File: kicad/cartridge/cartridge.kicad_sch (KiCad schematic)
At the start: 11 parts, among them J1 Card edge (87715-9106 mate), U1 ATF22V10C-10PU, U2 AT28C256-15PU, U3 AT28C256-15PU, U4 AS7C256C-15PCN, U5 AS7C256C-15PCN

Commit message: KiCad schematic: wire each sheet's nets, one routed bus per bus, PLD names
A net with two or more pins on a sheet is now wired pin to pin by a small
grid router (src/scripts/kicad_route.py) instead of a label per pin.
Numbered groups (D, A, SRC, PC, ...) are drawn as one bus per sheet with
bus entries, routed between the chips and named by one bus label.  Each
PLD shows its job under its part number.  Netlist check: 0 problems.

Co-Authored-By: Claude Opus 5.5 (1M context) <noreply@anthropic.com>
Claude-Session: https://claude.ai/code/session_01L9AkLuEg13EebxDmgXsaEp
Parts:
- U1: Function (none) -> Loader PLD
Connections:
- net HOLD: no longer names the net of J1.B18 (HOLD), U1.23 (/RELEASE)
- net OSC: no longer names the net of J1.A20 (OSC), U1.1 (OSC)
- net PIXEL_ENABLE: no longer names the net of J1.A18 (PIXEL_ENABLE), U1.3 (PIXEL_ENABLE)
- net RUN: no longer names the net of J1.A19 (RUN), U1.22 (RUN)
- net ~{CE_HI}: no longer names the net of J1.B16 (/CE_HI), U3.20 (~{CS}), U5.20 (/CE)
- net ~{CE_LO}: no longer names the net of J1.A16 (/CE_LO), U1.2 (A15), U2.20 (~{CS}), U4.20 (/CE)
- net ~{EE_OE}: no longer names the net of U1.20 (/EE_OE), U2.22 (~{OE}), U3.22 (~{OE})
- net ~{ROM_OE}: no longer names the net of J1.A17 (/ROM_OE), U4.22 (/OE), U5.22 (/OE)
- net ~{SRC_EN}: no longer names the net of J1.B17 (/SRC_EN), U1.4 (/SRC_EN)
- net ~{SR_WE}: no longer names the net of U1.19 (/SR_WE), U4.27 (/WE), U5.27 (/WE)

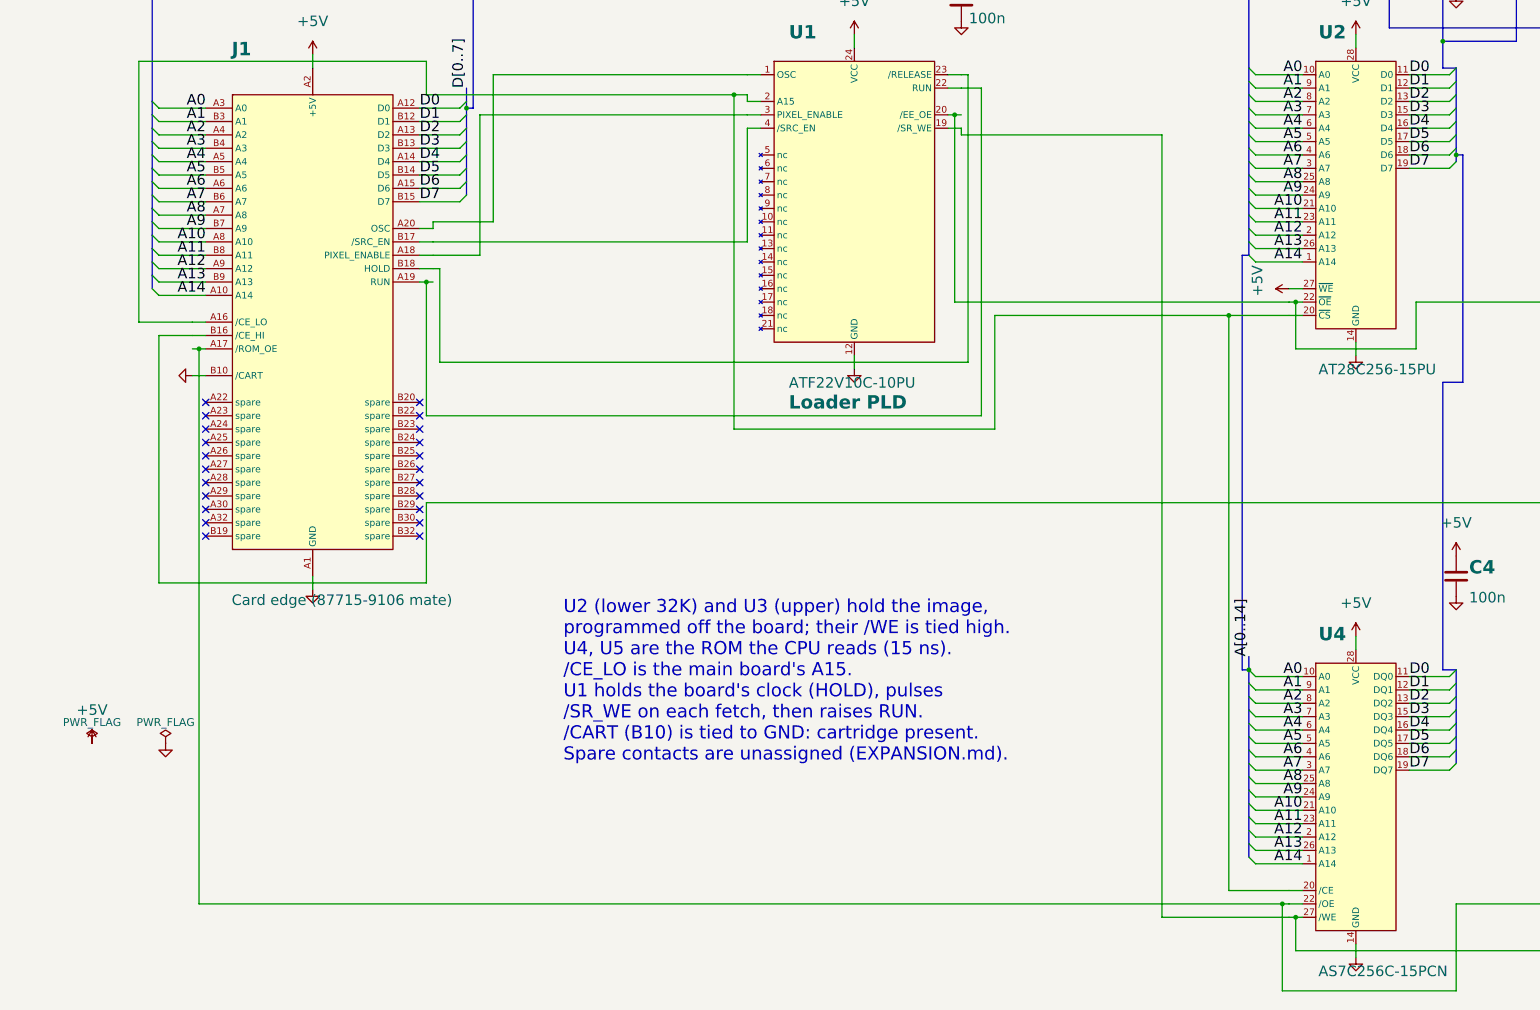
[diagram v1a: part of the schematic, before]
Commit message: Revert the opcode XOR: plain encoding, the cartridge 74AC541 is back
Justin found the inverted opcode bytes too confusing, and a pulled-low
bus is not practical, so this undoes 63a428c:
- opcode bytes are the plain fields again (nop = 02h); the cartridge's
  74AC541 drives 02h while it loads (6 chips, about 33 ms)
- State and Branch PLD revision 15, ALU revision 07 and cartridge PLD
  revision 03 have the same logic as 13, 13, 05 and 01
- read bus pull-ups 10k again; bring-up colour pull-downs 1k
- cartridge schematic gets U6 (74AC541), data bus SIP 10k
- program hex, menu ROM and bring-up ROM reassembled

Kept from 63a428c: RUN starts high in basys_top, the bring-up ROM's
explicit jump to frame_loop, and test_io's con_gets ROM map.

Co-Authored-By: Claude Opus 5.5 (1M context) <noreply@anthropic.com>
Claude-Session: https://claude.ai/code/session_01PNJoPfzmo1tu8EorCrua96
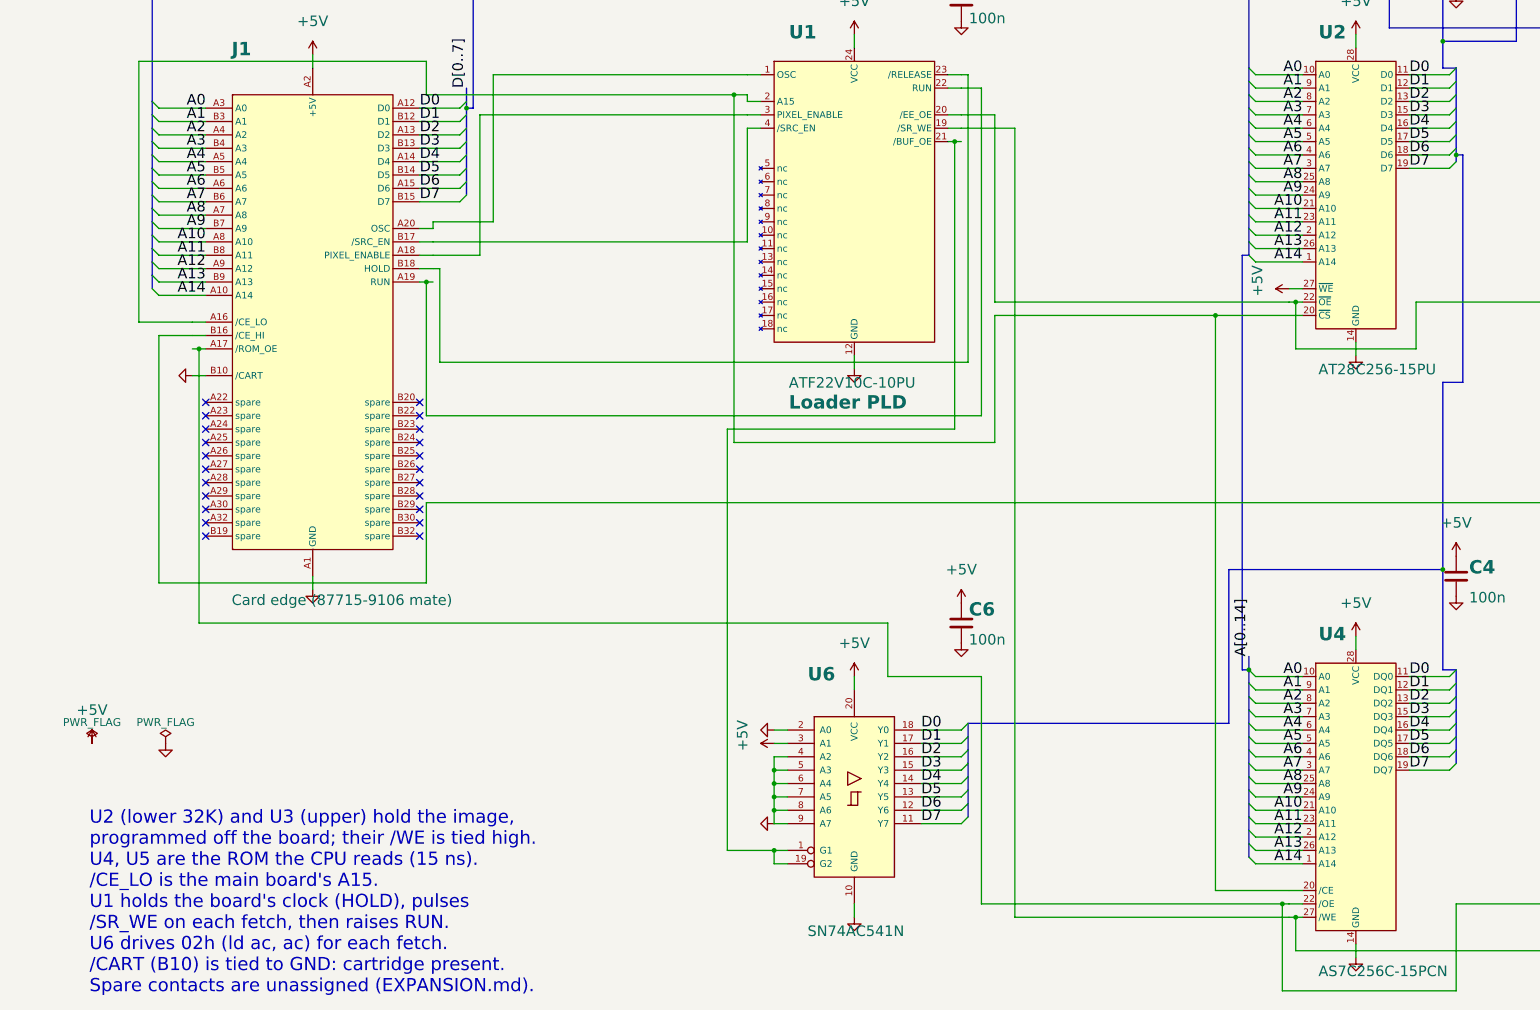
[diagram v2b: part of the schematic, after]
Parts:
- added C6: 100n, Capacitor_THT:C_Disc_D5.0mm_W2.5mm_P5.00mm, symbol Device:C
- added U6: SN74AC541N, Package_DIP:DIP-20_W7.62mm, symbol 74xx:74LS541
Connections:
- net +5V: now also C6.1, U6.20 (VCC), U6.3 (A1)
- net D0: now also U6.18 (Y0)
- net D1: now also U6.17 (Y1)
- net D2: now also U6.16 (Y2)
- net D3: now also U6.15 (Y3)
- net D4: now also U6.14 (Y4)
- net D5: now also U6.13 (Y5)
- net D6: now also U6.12 (Y6)
- net D7: now also U6.11 (Y7)
- net GND: now also C6.2, U6.10 (GND), U6.2 (A0), U6.4 (A2), U6.5 (A3), U6.6 (A4), U6.7 (A5), U6.8 (A6), U6.9 (A7)
- net at U1.21 (/BUF_OE): now also U6.1 (G1), U6.19 (G2)
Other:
- note added: "U6 drives 02h (ld ac, ac) for each fetch."

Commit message: Cartridge loader everywhere: FPGA cartridge model, random RAM, nop at x0000
- src/hdl/cartridge.vhd: the ROM cartridge (loader PLD, EEPROMs from
  rom.mem, SRAM written by /SR_WE); basys_top uses it for RUN, STALL_OUT
  and the ROM data, and the IR PLD replaces the instruction F377
- main RAM and cartridge SRAM start random (gen_random_ram.tcl writes
  ram.mem and cart_ram.mem); build, fast and create_project scripts
  updated, new .vhd files are added to an existing project
- rom_boot and the bring-up ROM keep a nop at x0000 for the hand-off;
  menu and bring-up images rebuilt
- schematic: IR PLD as U17, no 74AC32, STALL_IN/STALL_OUT/PC_ENABLE on
  the cartridge connector, cartridge without the 541; PDFs regenerated
- docs: ROM, CHIPS, BRINGUP, EXPANSION, timing, PLD usage, kitting,
  schematic plan, block diagram
- src/sim/tb_top_load.vhd: whole FPGA model from power-up through the
  load and boot

Co-Authored-By: Claude Opus 5.5 (1M context) <noreply@anthropic.com>
Claude-Session: https://claude.ai/code/session_01PNJoPfzmo1tu8EorCrua96
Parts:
- removed C6: 100n, Capacitor_THT:C_Disc_D5.0mm_W2.5mm_P5.00mm, symbol Device:C
- removed U6: SN74AC541N, Package_DIP:DIP-20_W7.62mm, symbol 74xx:74LS541
- U1: value ATF22V10C-10PU -> ATF22V10C-7PX
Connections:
- net at J1.B17 (STALL_IN): now also U1.5 (STALL_IN); no longer U1.4 (/SRC_EN)
- net at J1.B19 (PC_ENABLE): now also U1.4 (PC_ENABLE)
- no-connect marks 22 -> 21
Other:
- note added: "(STALL_OUT), pulses /SR_WE, lets the CPU"
- note added: "U1 stalls the CPU at each PC address"
- note added: "step, and raises RUN when the PC wraps."
- note removed: "/SR_WE on each fetch, then raises RUN."
- note removed: "U1 holds the board's clock (HOLD), pulses"
- note removed: "U6 drives 02h (ld ac, ac) for each fetch."

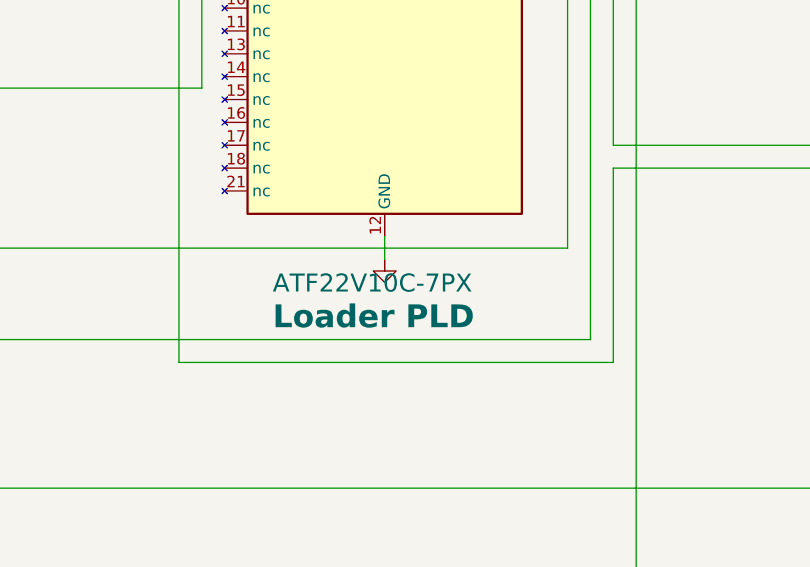
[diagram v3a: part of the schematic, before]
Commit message: Branch, audio slot and cartridge PLDs to ATF22V10C-10PU
The IR PLD's 5.5 ns clock to output gave the IR-started paths 5 ns, so
the Branch PLD (+4.7 branch decision, +2.2 STALL through the cartridge)
and the audio slot PLD (+5.2 /AC_SEL) fit the -10 grade; the cartridge
loader goes with them (tb_cart_load passes with every PLD at -10).

Co-Authored-By: Claude Opus 5.5 (1M context) <noreply@anthropic.com>
Claude-Session: https://claude.ai/code/session_01PNJoPfzmo1tu8EorCrua96
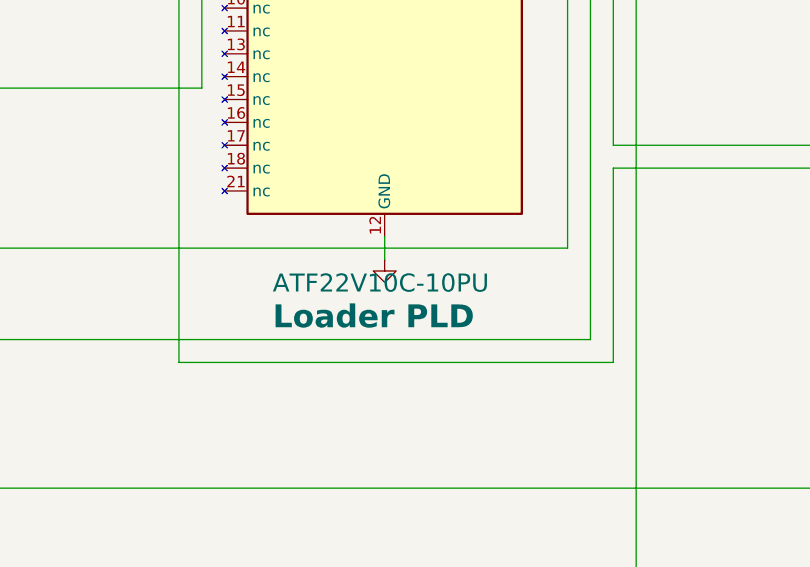
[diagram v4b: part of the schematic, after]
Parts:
- U1: value ATF22V10C-7PX -> ATF22V10C-10PU
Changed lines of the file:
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@@
   (wire (pts (xy 175.26 125.73) (xy 175.26 128.27)) (stroke (width 0) (type default)))
   (symbol (lib_id "power:GND") (at 175.26 128.27 0) (unit 1) (in_bom yes) (on_board yes) (dnp no) (property "Reference" "#PWR0105" (at 175.26 128.27 0) (effects (font (size 1.27 1.27)) hide)) (property "Value" "GND" (at 175.26 134.62 0) (effects (font (size 2 2)) hide)) (property "Footprint" "" (at 175.26 128.27 0) (effects (font (size 1.27 1.27)) hide)) (property "Datasheet" "" (at 175.26 128.27 0) (effects (font (size 1.27 1.27)) hide)) (pin "1") (instances (project "cartridge" (path "/58e6aaf0-b096-58ec-a49b-041f90960c95" (reference "#PWR0105") (unit 1)))))
-  (symbol (lib_id "placard:ATF22V10C_CART") (at 175.26 95.25 0) (unit 1) (in_bom yes) (on_board yes) (dnp no) (property "Reference" "U1" (at 162.814 63.27 0) (effects (font (size 2.54 2.54) bold) (justify left bottom))) (property "Value" "ATF22V10C-7PX" (at 162.814 129.73 0) (effects (font (size 2 2)) (justify left top))) (property "Function" "Loader PLD" (at 162.814 133.13 0) (effects (font (size 2.54 2.54) bold) (justify left top))) (property "Footprint" "Package_DIP:DIP-24_W7.62mm" (at 175.26 95.25 0) (effects (font (size 1.27 1.27)) hide)) (property "Datasheet" "https://ww1.microchip.com/downloads/en/DeviceDoc/doc0735.pdf" (at 175.26 95.25 0) (effects (font (size 1.27 1.27)) hide)) (property "PLD" "ATF22V10_CART.pld" (at 175.26 95.25 0) (effects (font (size 1.27 1.27)) hide)) (pin "1") (pin "2") (pin "3") (pin "4") (pin "5") (pin "6") (pin "7") (pin "8") (pin "9") (pin "10") (pin "11") (pin "13") (pin "14") (pin "15") (pin "16") (pin "17") (pin "18") (pin "21") (pin "22") (pin "20") (pin "19") (pin "23") (pin "24") (pin "12") (instances (project "cartridge" (path "/58e6aaf0-b096-58ec-a49b-041f90960c95" (reference "U1") (unit 1)))))
+  (symbol (lib_id "placard:ATF22V10C_CART") (at 175.26 95.25 0) (unit 1) (in_bom yes) (on_board yes) (dnp no) (property "Reference" "U1" (at 162.814 63.27 0) (effects (font (size 2.54 2.54) bold) (justify left bottom))) (property "Value" "ATF22V10C-10PU" (at 162.814 129.73 0) (effects (font (size 2 2)) (justify left top))) (property "Function" "Loader PLD" (at 162.814 133.13 0) (effects (font (size 2.54 2.54) bold) (justify left top))) (property "Footprint" "Package_DIP:DIP-24_W7.62mm" (at 175.26 95.25 0) (effects (font (size 1.27 1.27)) hide)) (property "Datasheet" "https://ww1.microchip.com/downloads/en/DeviceDoc/doc0735.pdf" (at 175.26 95.25 0) (effects (font (size 1.27 1.27)) hide)) (property "PLD" "ATF22V10_CART.pld" (at 175.26 95.25 0) (effects (font (size 1.27 1.27)) hide)) (pin "1") (pin "2") (pin "3") (pin "4") (pin "5") (pin "6") (pin "7") (pin "8") (pin "9") (pin "10") (pin "11") (pin "13") (pin "14") (pin "15") (pin "16") (pin "17") (pin "18") (pin "21") (pin "22") (pin "20") (pin "19") (pin "23") (pin "24") (pin "12") (instances (project "cartridge" (path "/58e6aaf0-b096-58ec-a49b-041f90960c95" (reference "U1") (unit 1)))))
   (symbol (lib_id "power:+5V") (at 195.58 54.61 0) (unit 1) (in_bom yes) (on_board yes) (dnp no) (property "Reference" "#PWR0106" (at 195.58 54.61 0) (effects (font (size 1.27 1.27)) hide)) (property "Value" "+5V" (at 195.58 48.26 0) (effects (font (size 2 2)))) (property "Footprint" "" (at 195.58 54.61 0) (effects (font (size 1.27 1.27)) hide)) (property "Datasheet" "" (at 195.58 54.61 0) (effects (font (size 1.27 1.27)) hide)) (pin "1") (instances (project "cartridge" (path "/58e6aaf0-b096-58ec-a49b-041f90960c95" (reference "#PWR0106") (unit 1)))))
   (symbol (lib_id "power:GND") (at 195.58 62.23 0) (unit 1) (in_bom yes) (on_board yes) (dnp no) (property "Reference" "#PWR0107" (at 195.58 62.23 0) (effects (font (size 1.27 1.27)) hide)) (property "Value" "GND" (at 195.58 68.58 0) (effects (font (size 2 2)) hide)) (property "Footprint" "" (at 195.58 62.23 0) (effects (font (size 1.27 1.27)) hide)) (property "Datasheet" "" (at 195.58 62.23 0) (effects (font (size 1.27 1.27)) hide)) (pin "1") (instances (project "cartridge" (path "/58e6aaf0-b096-58ec-a49b-041f90960c95" (reference "#PWR0107") (unit 1)))))
